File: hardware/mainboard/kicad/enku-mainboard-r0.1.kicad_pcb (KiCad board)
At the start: 4 copper layers, 54 x 94 mm, 122 parts, among them J1 1S LiPo + NTC, J2 Hirose DM3AT-SF-PEJM5, J3 FH34SRJ-24S-0.5SH(50), J5 GCT USB4105-GF-A-120, J6 4-pin pogo dock, J7 Tag-Connect TC2030-IDC-NL, Q1 IRLML6346TRPBF, SW1 HARD POWER, SW2 BOOT / RECOVERY, SW3 BTN_L1, SW4 BTN_L2, SW5 BTN_R1, SW6 BTN_R2, U1 ESP32-S3-WROOM-1-N16R8, U2 TPS2121, U3 BQ25185DLHR, U4 TPS63802DLAR, U5 BMI270, U6 DRV5032FBDBZR, U8 USBLC6-2SC6

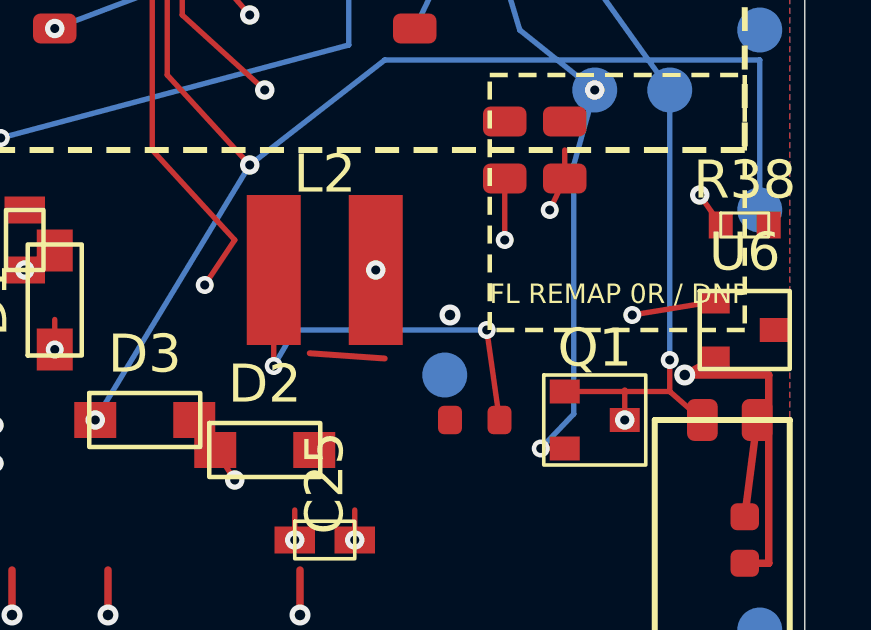
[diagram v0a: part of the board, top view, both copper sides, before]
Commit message: pcb: remove obsolete Hall supply transition
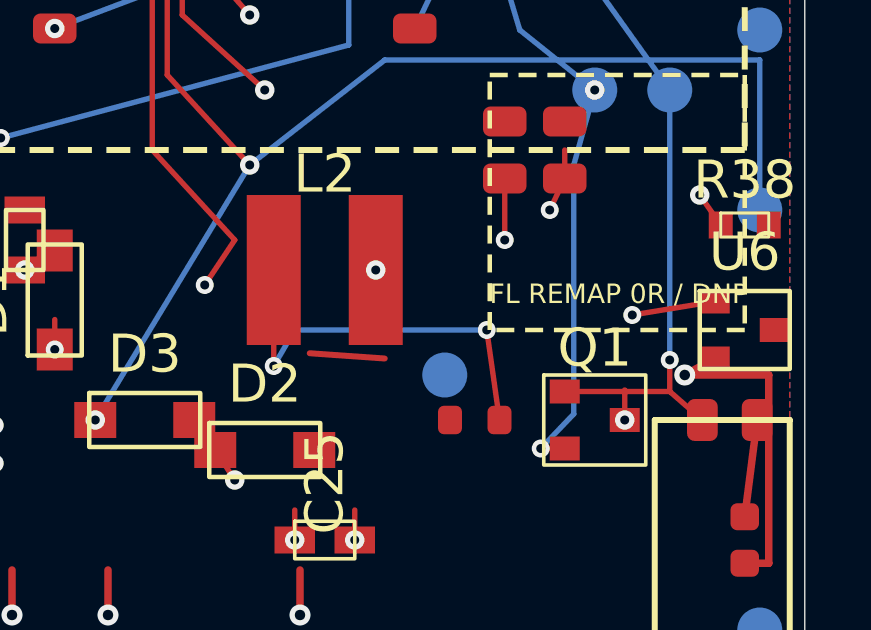
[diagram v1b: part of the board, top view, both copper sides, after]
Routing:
- net 3V3_SYS: vias 19 -> 18
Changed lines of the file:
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@@
   (segment (start 28.000 86.825) (end 28.000 89.825) (width 0.25) (layer "F.Cu") (net 80))
   (segment (start 62.175 44.500) (end 57.175 54.500) (width 0.25) (layer "In2.Cu") (net 2))
-  (via (at 62.175 44.500) (size 0.70) (drill 0.35) (layers "F.Cu" "In2.Cu") (net 2))
   (segment (start 71.000 45.950) (end 70.000 46.500) (width 0.25) (layer "F.Cu") (net 2))
   (segment (start 72.000 52.775) (end 72.800 52.775) (width 0.25) (layer "F.Cu") (net 2))

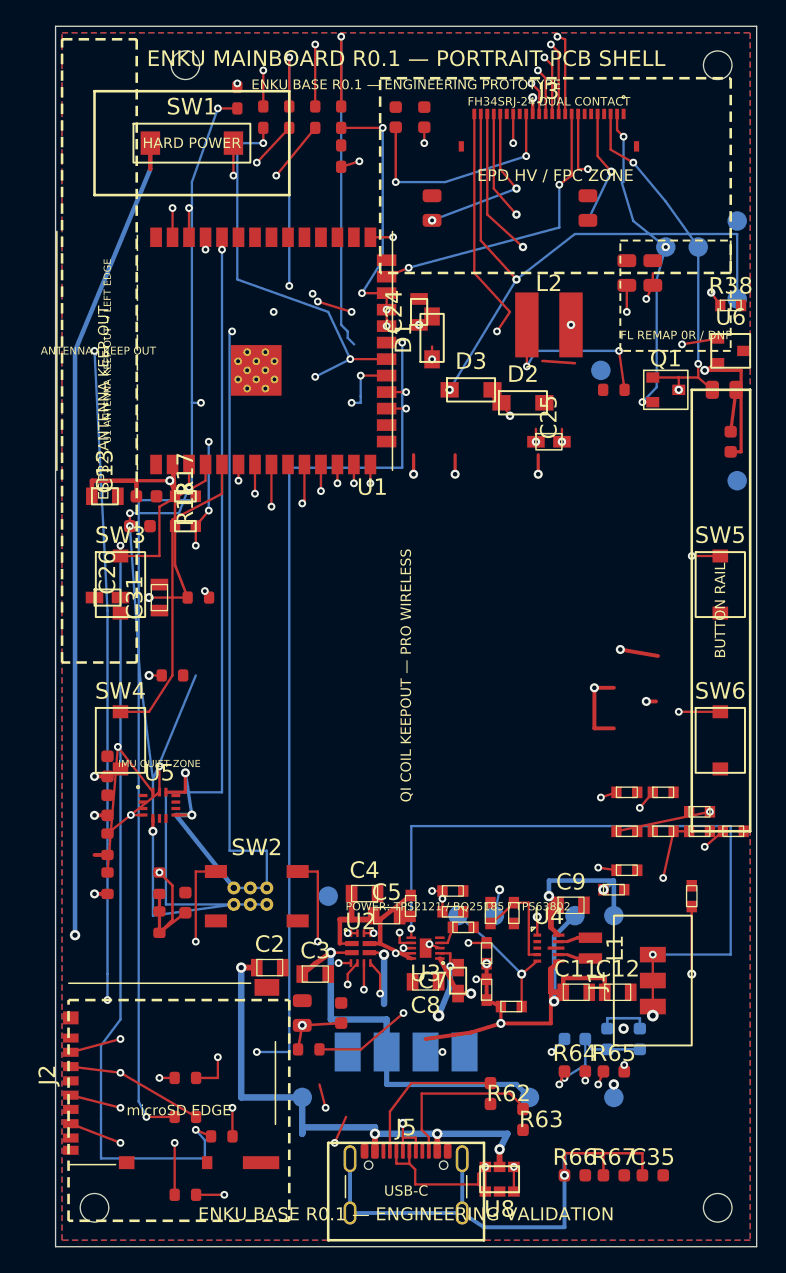
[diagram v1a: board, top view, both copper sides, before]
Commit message: pcb: close explicit layer-transition gaps
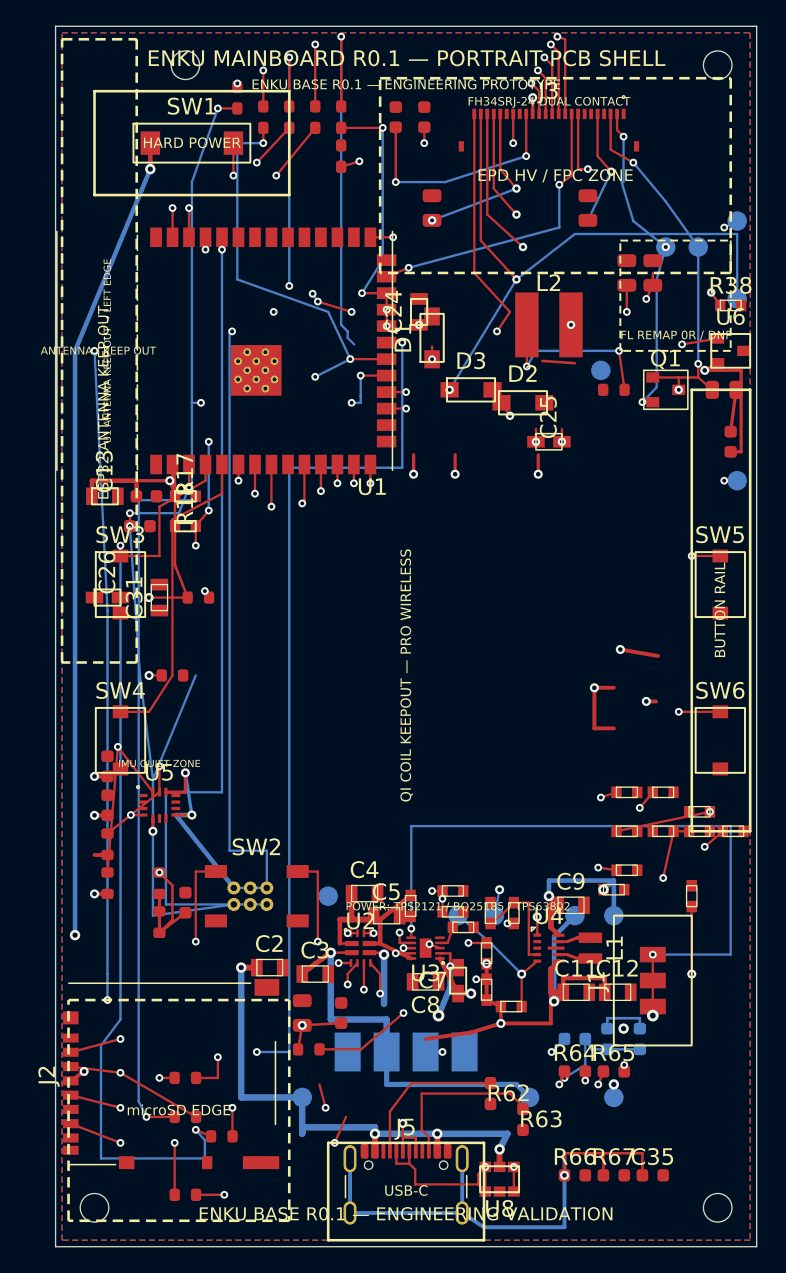
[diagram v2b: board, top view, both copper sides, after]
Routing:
- net EPD_VCOM: track 49.4 -> 50.6 mm, vias 2 -> 3
- net SPI_MOSI: track 113.7 -> 114.5 mm
- net 3V3_SYS: track 275.3 -> 276.0 mm, vias 18 -> 20
- net EPD_VGH: track 54.5 -> 55.2 mm, vias 2 -> 3
- net VSYS: vias 7 -> 8
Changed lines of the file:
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@@
   (segment (start 53.200 95.000) (end 53.200 92.200) (width 0.30) (layer "F.Cu") (net 2))
   (via (at 53.200 92.200) (size 0.70) (drill 0.35) (layers "F.Cu" "In2.Cu") (net 2))
-  (segment (start 53.200 92.200) (end 55.300 89.100) (width 0.25) (layer "In2.Cu") (net 2))
+  (segment (start 53.200 92.200) (end 54.800 89.100) (width 0.25) (layer "In2.Cu") (net 2))
+  (via (at 54.800 89.100) (size 0.60) (drill 0.30) (layers "F.Cu" "In2.Cu") (net 2))
+  (segment (start 54.800 89.100) (end 55.300 89.100) (width 0.25) (layer "F.Cu") (net 2))
   (via (at 39.000 96.950) (size 0.70) (drill 0.35) (layers "F.Cu" "In2.Cu") (net 2))
   (segment (start 52.000 97.500) (end 54.300 96.800) (width 0.30) (layer "F.Cu") (net 2))
   (segment (start 23.000 86.825) (end 23.000 96.000) (width 0.30) (layer "In2.Cu") (net 2))
-  (segment (start 23.000 86.825) (end 21.175 101.225) (width 0.30) (layer "In2.Cu") (net 2))
+  (segment (start 23.000 86.825) (end 22.200 100.500) (width 0.30) (layer "In2.Cu") (net 2))
+  (via (at 22.200 100.500) (size 0.70) (drill 0.35) (layers "F.Cu" "In2.Cu") (net 2))
+  (segment (start 22.200 100.500) (end 21.175 101.225) (width 0.30) (layer "F.Cu") (net 2))
   (via (at 28.800 55.000) (size 0.70) (drill 0.35) (layers "F.Cu" "In2.Cu") (net 2))
   (segment (start 28.800 55.000) (end 47.575 54.500) (width 0.25) (layer "In2.Cu") (net 2))
@@
   (segment (start 64 42) (end 61 38) (width 0.18) (layer "In1.Cu") (net 27))
   (segment (start 61 38) (end 56 37) (width 0.18) (layer "In1.Cu") (net 27))
-  (segment (start 72.5 35) (end 72 38.5) (width 0.18) (layer "In2.Cu") (net 26))
-  (segment (start 72.5 55) (end 73 49) (width 0.18) (layer "In2.Cu") (net 29))
+  (segment (start 71.500 35.500) (end 72.000 38.500) (width 0.18) (layer "In2.Cu") (net 26))
+  (via (at 71.500 35.500) (size 0.60) (drill 0.30) (layers "In2.Cu" "B.Cu") (net 26))
+  (segment (start 71.500 35.500) (end 72.500 35.000) (width 0.18) (layer "B.Cu") (net 26))
+  (segment (start 71.500 55.000) (end 73.000 49.000) (width 0.18) (layer "In2.Cu") (net 29))
+  (via (at 71.500 55.000) (size 0.60) (drill 0.30) (layers "In2.Cu" "B.Cu") (net 29))
+  (segment (start 71.500 55.000) (end 72.500 55.000) (width 0.18) (layer "B.Cu") (net 29))
   (segment (start 73 49) (end 69.5 43) (width 0.18) (layer "In2.Cu") (net 29))
   (via (at 49 45.65) (size 0.60) (drill 0.30) (layers "F.Cu" "In1.Cu") (net 30))
@@
   (via (at 39.8 40.6) (size 0.60) (drill 0.30) (layers "F.Cu" "B.Cu") (net 61))
   (via (at 40.2 41.2) (size 0.60) (drill 0.30) (layers "F.Cu" "B.Cu") (net 61))
+  (segment (start 39.800 40.600) (end 40.200 41.200) (width 0.18) (layer "B.Cu") (net 61))
   (segment (start 40.2 41.2) (end 42.8 42.0) (width 0.18) (layer "F.Cu") (net 61))
   (via (at 42.8 42.0) (size 0.60) (drill 0.30) (layers "F.Cu" "B.Cu") (net 61))
@@
   (segment (start 22.000 82.000) (end 28.000 85.175) (width 0.18) (layer "In2.Cu") (net 73))
   (via (at 28.000 85.175) (size 0.60) (drill 0.30) (layers "F.Cu" "In2.Cu") (net 73))
+  (via (at 27.300 31.000) (size 0.80) (drill 0.40) (layers "F.Cu" "B.Cu") (net 32))
   (segment (start 27.300 31.000) (end 21.500 45.000) (width 0.35) (layer "B.Cu") (net 32))
   (segment (start 21.500 45.000) (end 21.500 90.000) (width 0.35) (layer "B.Cu") (net 32))

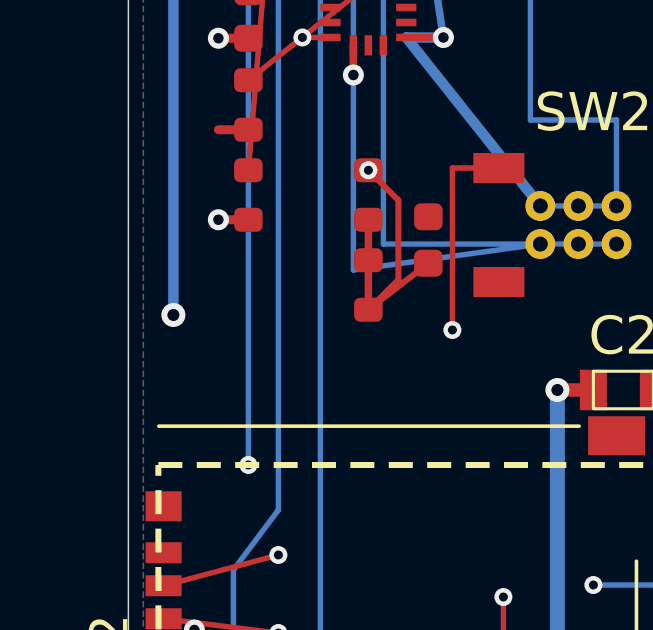
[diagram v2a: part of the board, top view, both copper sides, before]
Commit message: pcb: separate VSYS transition from USB D-
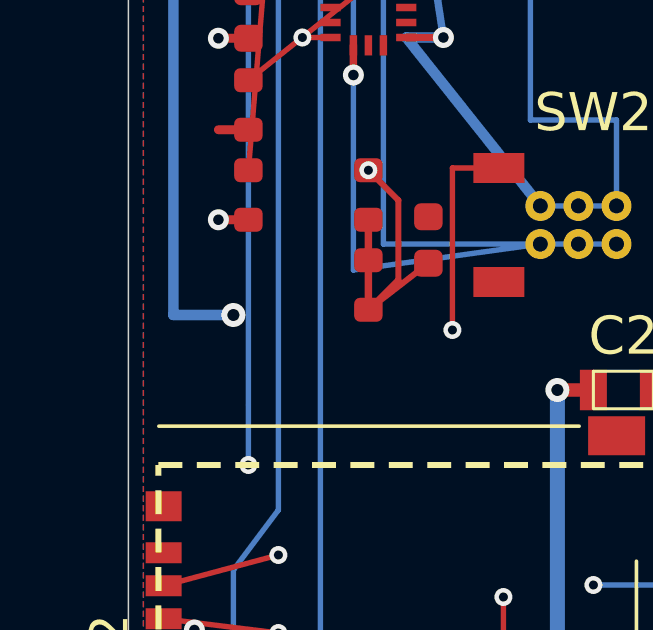
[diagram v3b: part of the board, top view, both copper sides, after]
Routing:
- net VSYS: track 168.4 -> 169.4 mm
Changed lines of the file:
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@@
   (segment (start 27.300 31.000) (end 21.500 45.000) (width 0.35) (layer "B.Cu") (net 32))
   (segment (start 21.500 45.000) (end 21.500 90.000) (width 0.35) (layer "B.Cu") (net 32))
-  (via (at 21.500 90.000) (size 0.80) (drill 0.40) (layers "B.Cu" "In1.Cu") (net 32))
-  (segment (start 21.500 90.000) (end 25.000 94.500) (width 0.35) (layer "In1.Cu") (net 32))
+  (segment (start 21.500 90.000) (end 23.500 90.000) (width 0.35) (layer "B.Cu") (net 32))
+  (via (at 23.500 90.000) (size 0.80) (drill 0.40) (layers "B.Cu" "In1.Cu") (net 32))
+  (segment (start 23.500 90.000) (end 25.000 94.500) (width 0.35) (layer "In1.Cu") (net 32))
   (segment (start 25.000 94.500) (end 52.000 94.500) (width 0.35) (layer "In1.Cu") (net 32))
   (segment (start 60.800 98.000) (end 61.300 98.800) (width 0.20) (layer "B.Cu") (net 72))

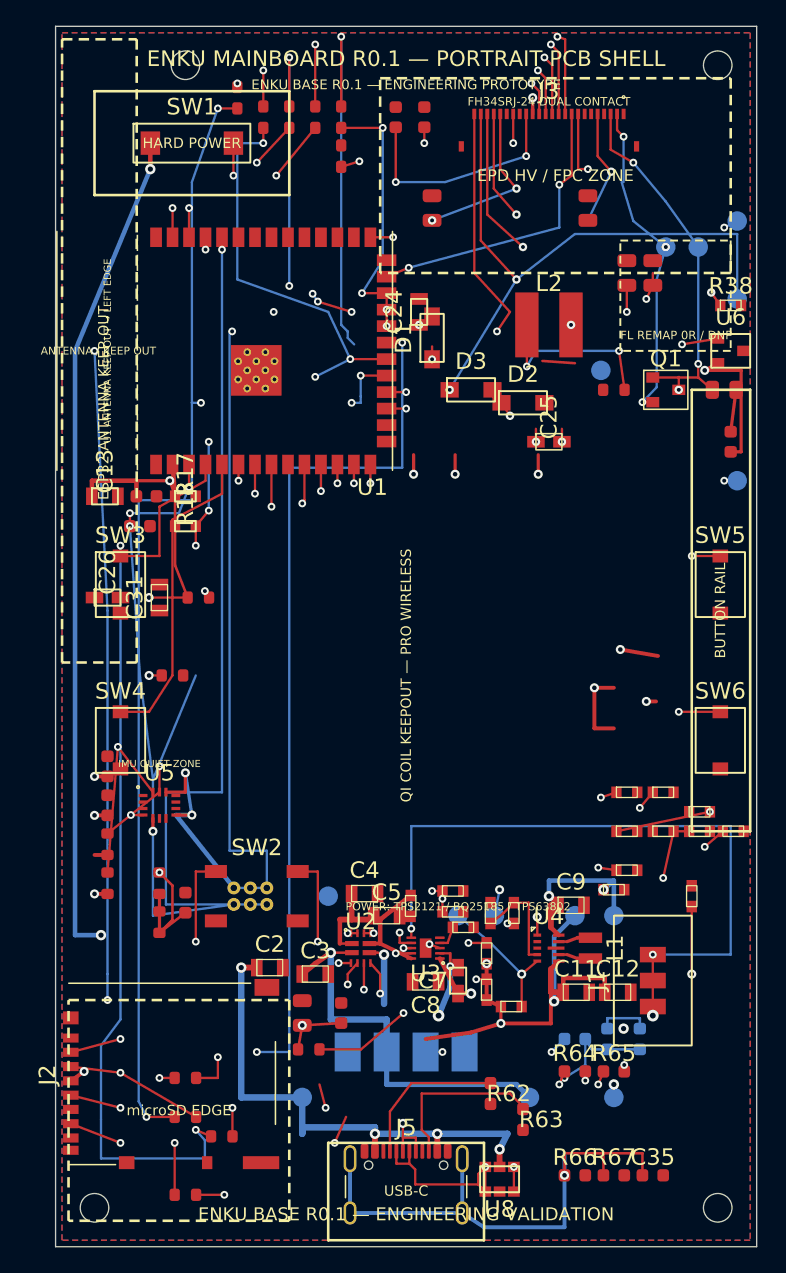
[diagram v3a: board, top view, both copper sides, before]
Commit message: pcb: reroute SD CS dock detect and EPD RESE
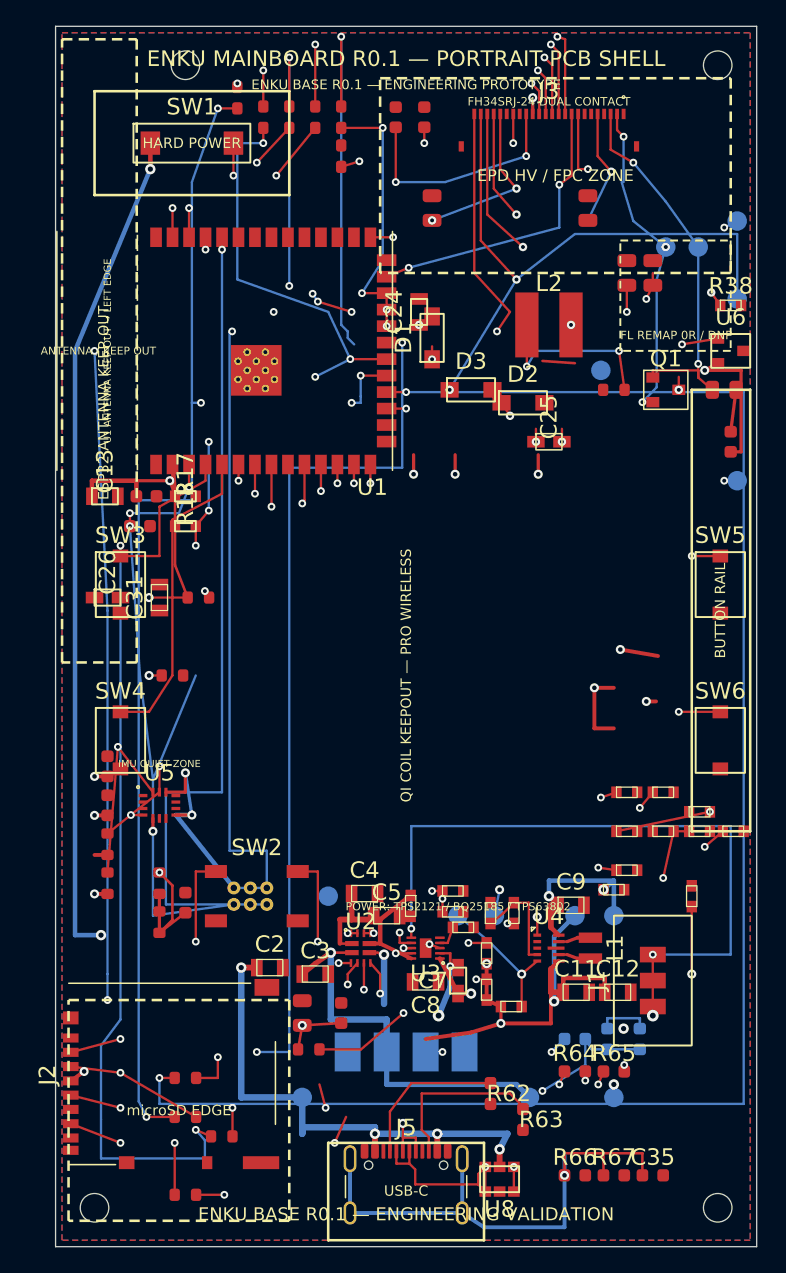
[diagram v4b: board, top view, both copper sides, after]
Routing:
- net SD_CS: track 91.8 -> 130.5 mm
- net EPD_RESE: track 28.0 -> 29.1 mm
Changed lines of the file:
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@@
   (segment (start 25.800 80.750) (end 26.7375 80.7500) (width 0.18) (layer "F.Cu") (net 55))
   (segment (start 45.500 48.175) (end 47.000 48.175) (width 0.18) (layer "F.Cu") (net 60))
-  (via (at 47.000 48.175) (size 0.60) (drill 0.30) (layers "F.Cu" "In1.Cu") (net 60))
-  (segment (start 47.000 48.175) (end 40.000 48.175) (width 0.18) (layer "In1.Cu") (net 60))
-  (segment (start 40.000 48.175) (end 40.000 47.000) (width 0.18) (layer "In1.Cu") (net 60))
-  (segment (start 40.000 47.000) (end 20.500 47.000) (width 0.18) (layer "In1.Cu") (net 60))
-  (segment (start 20.500 47.000) (end 20.500 101.000) (width 0.18) (layer "In1.Cu") (net 60))
-  (segment (start 20.500 101.000) (end 28.000 101.000) (width 0.18) (layer "In1.Cu") (net 60))
-  (via (at 28.000 101.000) (size 0.60) (drill 0.30) (layers "F.Cu" "In1.Cu") (net 60))
+  (via (at 47.000 48.175) (size 0.60) (drill 0.30) (layers "F.Cu" "B.Cu") (net 60))
+  (segment (start 47.000 48.175) (end 73.000 48.175) (width 0.18) (layer "B.Cu") (net 60))
+  (segment (start 73.000 48.175) (end 73.000 103.000) (width 0.18) (layer "B.Cu") (net 60))
+  (segment (start 73.000 103.000) (end 28.000 103.000) (width 0.18) (layer "B.Cu") (net 60))
+  (segment (start 28.000 103.000) (end 28.000 101.000) (width 0.18) (layer "B.Cu") (net 60))
+  (via (at 28.000 101.000) (size 0.60) (drill 0.30) (layers "F.Cu" "B.Cu") (net 60))
   (segment (start 28.000 101.000) (end 29.175 101.000) (width 0.18) (layer "F.Cu") (net 60))
   (segment (start 41.71 53.75) (end 41.71 55.20) (width 0.18) (layer "F.Cu") (net 56))
@@
   (segment (start 54 47) (end 57 52) (width 0.18) (layer "In1.Cu") (net 30))
   (segment (start 42 27.825) (end 45.2 27.825) (width 0.18) (layer "F.Cu") (net 66))
-  (segment (start 66 47.05) (end 69.5 47.05) (width 0.18) (layer "F.Cu") (net 14))
+  (segment (start 66.000 47.050) (end 66.000 46.500) (width 0.18) (layer "F.Cu") (net 14))
+  (segment (start 66.000 46.500) (end 69.500 46.500) (width 0.18) (layer "F.Cu") (net 14))
+  (segment (start 69.500 46.500) (end 69.500 47.050) (width 0.18) (layer "F.Cu") (net 14))
   (segment (start 69.5 47.05) (end 70.5875 48) (width 0.18) (layer "F.Cu") (net 14))
   (segment (start 65.5 41.0) (end 66 39.95) (width 0.18) (layer "F.Cu") (net 29))
@@
   (segment (start 24.000 93.000) (end 24.000 95.000) (width 0.18) (layer "B.Cu") (net 72))
   (via (at 24.000 95.000) (size 0.60) (drill 0.30) (layers "B.Cu" "In2.Cu") (net 72))
-  (segment (start 24.000 95.000) (end 59.200 101.000) (width 0.18) (layer "In2.Cu") (net 72))
-  (via (at 59.200 101.000) (size 0.60) (drill 0.30) (layers "B.Cu" "In2.Cu") (net 72))
-  (segment (start 59.200 101.000) (end 60.800 100.000) (width 0.18) (layer "B.Cu") (net 72))
+  (segment (start 24.000 95.000) (end 57.500 102.000) (width 0.18) (layer "In2.Cu") (net 72))
+  (via (at 57.500 102.000) (size 0.60) (drill 0.30) (layers "B.Cu" "In2.Cu") (net 72))
+  (segment (start 57.500 102.000) (end 60.800 100.000) (width 0.18) (layer "B.Cu") (net 72))
   (segment (start 60.800 100.000) (end 60.800 98.000) (width 0.18) (layer "B.Cu") (net 72))
   (segment (start 31.550 55.000) (end 28.000 57.000) (width 0.18) (layer "F.Cu") (net 48))
